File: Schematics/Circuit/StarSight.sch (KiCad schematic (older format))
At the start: 1 part

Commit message: Add last year code and schematic base
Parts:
- removed SH?: ARDUINO_MEGA, symbol ARDUINO_MEGA
- added P?: CONN_13X2, Pin_Headers:Pin_Header_Straight_2x13, symbol CONN_13X2
- added SH?: ARDUINO_MEGA, symbol ARDUINO_MEGA
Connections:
- net labels added: +3.3V, +5V, GND, GPIO0(SDA), GPIO1(SCL), GPIO10(MOSI), GPIO11(SCLK), GPIO17, GPIO18, GPIO21, GPIO22, GPIO23, GPIO24, GPIO25, GPIO4, GPIO7(CE1), GPIO8(CE0), GPIO9(MISO), RXD, TXD
- wire segments 0 -> 23
- no-connect marks 0 -> 6
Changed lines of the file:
@@
 LIBS:shield_arduino
 LIBS:StarSight-cache
+LIBS:raspberrypi-gpio-cache
 EELAYER 27 0
 EELAYER END
@@
 Sheet 1 1
 Title ""
-Date "14 dec 2017"
+Date "17 dec 2017"
 Rev ""
 Comp ""
@@
 $Comp
 L ARDUINO_MEGA SH?
-U 1 1 5A3242BC
-P 3200 4000
-F 0 "SH?" H 3200 4525 60  0000 C CNN
-F 1 "ARDUINO_MEGA" H 3200 4725 60  0000 C CNN
-F 2 "" H 2250 4300 60  0000 C CNN
-F 3 "" H 2250 4300 60  0000 C CNN
-	1    3200 4000
+U 1 1 5A367445
+P 8450 3450
+F 0 "SH?" H 8450 3975 60  0000 C CNN
+F 1 "ARDUINO_MEGA" H 8450 4175 60  0000 C CNN
+F 2 "" H 7500 3750 60  0000 C CNN
+F 3 "" H 7500 3750 60  0000 C CNN
+	1    8450 3450
 	1    0    0    -1
 $EndComp
+$Comp
+L CONN_13X2 P?
+U 1 1 5A367446
+P 2400 1800
+F 0 "P?" H 2400 2500 60  0000 C CNN
+F 1 "CONN_13X2" V 2400 1800 50  0000 C CNN
+F 2 "Pin_Headers:Pin_Header_Straight_2x13" H 2400 1100 30  0000 C CNN
+F 3 "" H 2400 1800 60  0001 C CNN
+	1    2400 1800
+	1    0    0    -1
+$EndComp
+$Comp
+L +3.3V #PWR?
+U 1 1 5A367447
+P 1900 1050
+F 0 "#PWR?" H 1900 900 50  0001 C CNN
+F 1 "+3.3V" H 1900 1190 50  0000 C CNN
+F 2 "" H 1900 1050 50  0000 C CNN
+F 3 "" H 1900 1050 50  0000 C CNN
+	1    1900 1050
+	1    0    0    -1
+$EndComp
+Wire Wire Line
+	1900 1050 1900 1200
+Wire Wire Line
+	1900 1200 2000 1200
+$Comp
+L +5V #PWR?
+U 1 1 5A367448
+P 2900 1050
+F 0 "#PWR?" H 2900 900 50  0001 C CNN
+F 1 "+5V" H 2900 1190 50  0000 C CNN
+F 2 "" H 2900 1050 50  0000 C CNN
+F 3 "" H 2900 1050 50  0000 C CNN
+	1    2900 1050
+	1    0    0    -1
+$EndComp
+Wire Wire Line
+	2900 1050 2900 1200
+Wire Wire Line
+	2900 1200 2800 1200
+NoConn ~ 2800 1300
+Wire Wire Line
+	2000 1300 1250 1300
+Wire Wire Line
+	2000 1400 1250 1400
+Text Label 1250 1300 0    60   ~ 0
+GPIO0(SDA)
+Text Label 1250 1400 0    60   ~ 0
+GPIO1(SCL)
+Wire Wire Line
+	2000 1500 1250 1500
+Text Label 1250 1500 0    60   ~ 0
+GPIO4
+NoConn ~ 2000 1600
+Wire Wire Line
+	2000 1700 1250 1700
+Wire Wire Line
+	2000 1800 1250 1800
+Wire Wire Line
+	2000 1900 1250 1900
+Text Label 1250 1700 0    60   ~ 0
+GPIO17
+Text Label 1250 1800 0    60   ~ 0
+GPIO21
+Text Label 1250 1900 0    60   ~ 0
+GPIO22
+NoConn ~ 2000 2000
+Wire Wire Line
+	2000 2100 1250 2100
+Wire Wire Line
+	2000 2200 1250 2200
+Wire Wire Line
+	2000 2300 1250 2300
+Text Label 1250 2100 0    60   ~ 0
+GPIO10(MOSI)
+Text Label 1250 2200 0    60   ~ 0
+GPIO9(MISO)
+Text Label 1250 2300 0    60   ~ 0
+GPIO11(SCLK)
+NoConn ~ 2000 2400
+$Comp
+L GND #PWR?
+U 1 1 5A367449
+P 2900 2500
+F 0 "#PWR?" H 2900 2250 50  0001 C CNN
+F 1 "GND" H 2900 2350 50  0000 C CNN
+F 2 "" H 2900 2500 50  0000 C CNN
+F 3 "" H 2900 2500 50  0000 C CNN
+	1    2900 2500
+	1    0    0    -1
+$EndComp
+Wire Wire Line
+	2900 2500 2900 1400
+Wire Wire Line
+	2900 1400 2800 1400
+Wire Wire Line
+	2800 1500 3500 1500
+Wire Wire Line
+	2800 1600 3500 1600
+Text Label 3500 1500 2    60   ~ 0
+TXD
+Text Label 3500 1600 2    60   ~ 0
+RXD
+Wire Wire Line
+	2800 1700 3500 1700
+Text Label 3500 1700 2    60   ~ 0
+GPIO18
+NoConn ~ 2800 1800
+Wire Wire Line
+	2800 1900 3500 1900
+Wire Wire Line
+	2800 2000 3500 2000
+Text Label 3500 1900 2    60   ~ 0
+GPIO23
+Text Label 3500 2000 2    60   ~ 0
+GPIO24
+NoConn ~ 2800 2100
+Wire Wire Line
+	2800 2200 3500 2200
+Text Label 3500 2200 2    60   ~ 0
+GPIO25
+Wire Wire Line
+	2800 2300 3500 2300
+Wire Wire Line
+	2800 2400 3500 2400
+Text Label 3500 2300 2    60   ~ 0
+GPIO8(CE0)
+Text Label 3500 2400 2    60   ~ 0
+GPIO7(CE1)
 $EndSCHEMATC

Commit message: Add the rest of the schematic
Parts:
- removed SH?: ARDUINO_MEGA, symbol ARDUINO_MEGA
- added C1, C2: 10 uF, ~, symbol C
- added C3: 100 nF, ~, symbol C
- added J1: Power, symbol Conn_01x02
- added J2: Line1, asd, symbol Conn_01x03
- added J3: Line2, asd, symbol Conn_01x03
- added J4: Line3, asd, symbol Conn_01x03
- added J5: Line4, asd, symbol Conn_01x03
- added J6: Line5, asd, symbol Conn_01x03
- added J? (x4): ultSound1, symbol Conn_01x04
- added J? (x5): IR1, asd, symbol Conn_01x03
- added SH?: ARDUINO_MEGA, symbol ARDUINO_MEGA
- added U?: LM1084IT-5.0/NOPB, TO-220, symbol LM1084IT-5.0/NOPB
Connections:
- net labels removed: +3.3V
- wire segments 23 -> 159
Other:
- moved on the sheet: P?

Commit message: Add pcb layout
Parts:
- removed J1: Power, symbol Conn_01x02
- removed SH?: ARDUINO_MEGA, symbol ARDUINO_MEGA
- added P2: Power, symbol CONN_2
- added SHIELD1: ARDUINO_MEGA_SHIELD, symbol ARDUINO_MEGA_SHIELD
- gave numbers to parts that had none: 11
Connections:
- wire segments 159 -> 165

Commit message: Add switched regulator and motors
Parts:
- removed U1: LM1084IT-5.0/NOPB, TO-220, symbol LM1084IT-5.0/NOPB
- added D1: 1n5824, symbol D_Schottky
- added D2, D3: D, Diodes_THT:D_DO-35_SOD27_P5.08mm_Vertical_KathodeUp, symbol D
- added IC1: LM2956-5V, symbol LM2956-5V
- added J16, J17: Conn_01x02, Pin_Headers:Pin_Header_Straight_1x02_Pitch2.54mm, symbol Conn_01x02
- added K1, K2: M1BS5V2-05T, Relays_THT:Relay_DPDT_Finder_40.52, symbol RSM822
- added L1: 33 uH, symbol L
- added Q1, Q2: Q_NMOS_GDS, Pin_Headers:Pin_Header_Straight_1x03_Pitch2.54mm, symbol Q_NMOS_GDS
- added R1, R2: 10k, Resistors_THT:R_Axial_DIN0207_L6.3mm_D2.5mm_P10.16mm_Horizontal, symbol R
- C1, C2, C3: symbol C -> C-RESCUE-StarSight
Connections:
- net GND: now also D1.2 (A), IC1.3 (GND), IC1.5 (ON/OFF), K1.11, K1.A1, K2.11, K2.A1, R1.1, R2.1
- net at C2.2, C3.2, P1.2 (P2): now also IC1.4 (FEEDBACK), L1.2
- net at SHIELD1.10: now also Q2.1 (G), R2.2
- net at SHIELD1.11: now also K2.A2
- net at SHIELD1.12: now also Q1.1 (G), R1.2
- net at SHIELD1.13: now also K1.A2
- net +12V: now reaches C1.2, P2.2 (PM), SHIELD1.V_IN
- net +12V: now also IC1.1 (VIN), Q1.3 (S), Q2.3 (S)
- new net: D1.1 (K), IC1.2 (OUT), L1.1
- new net: D2.2 (A), Q2.2 (D)
- new net: D2.1 (K), K2.21
- new net: J16.1 (Pin_1), K2.12, K2.24
- new net: J16.2 (Pin_2), K2.14, K2.22
- new net: J17.1 (Pin_1), K1.12, K1.24
- new net: J17.2 (Pin_2), K1.14, K1.22
- new net: D3.1 (K), K1.21
- new net: D3.2 (A), Q1.2 (D)
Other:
- moved on the sheet: C2, C3

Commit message: Fix footprint missing
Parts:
- D1: footprint (none) -> Diodes_THT:D_DO-201_P15.24mm_Horizontal
- IC1: footprint (none) -> Pin_Headers:Pin_Header_Straight_1x05_Pitch2.54mm
- L1: footprint (none) -> Diodes_THT:D_5W_P5.08mm_Vertical_KathodeUp
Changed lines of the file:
@@
 F 0 "IC1" H 2950 4050 60  0000 C CNN
 F 1 "LM2956-5V" H 3350 4050 60  0000 C CNN
-F 2 "" H 2950 4050 60  0001 C CNN
+F 2 "Pin_Headers:Pin_Header_Straight_1x05_Pitch2.54mm" H 2950 4050 60  0001 C CNN
 F 3 "" H 2950 4050 60  0001 C CNN
 	1    3250 3800
@@
 F 0 "L1" V 3100 4500 50  0000 C CNN
 F 1 "33 uH" V 3225 4500 50  0000 C CNN
-F 2 "" H 3150 4500 50  0001 C CNN
+F 2 "Diodes_THT:D_5W_P5.08mm_Vertical_KathodeUp" H 3150 4500 50  0001 C CNN
 F 3 "" H 3150 4500 50  0001 C CNN
 	1    3150 4500
@@
 F 0 "D1" H 2950 4450 50  0000 C CNN
 F 1 "1n5824" H 2950 4250 50  0000 C CNN
-F 2 "" H 2950 4350 50  0001 C CNN
+F 2 "Diodes_THT:D_DO-201_P15.24mm_Horizontal" H 2950 4350 50  0001 C CNN
 F 3 "" H 2950 4350 50  0001 C CNN
 	1    2950 4350

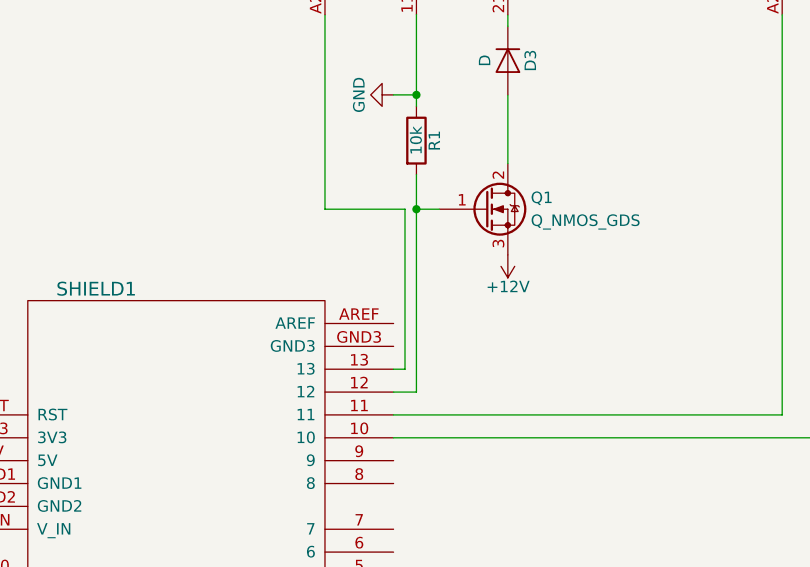
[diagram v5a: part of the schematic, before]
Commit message: Fix pcb power suply and motors
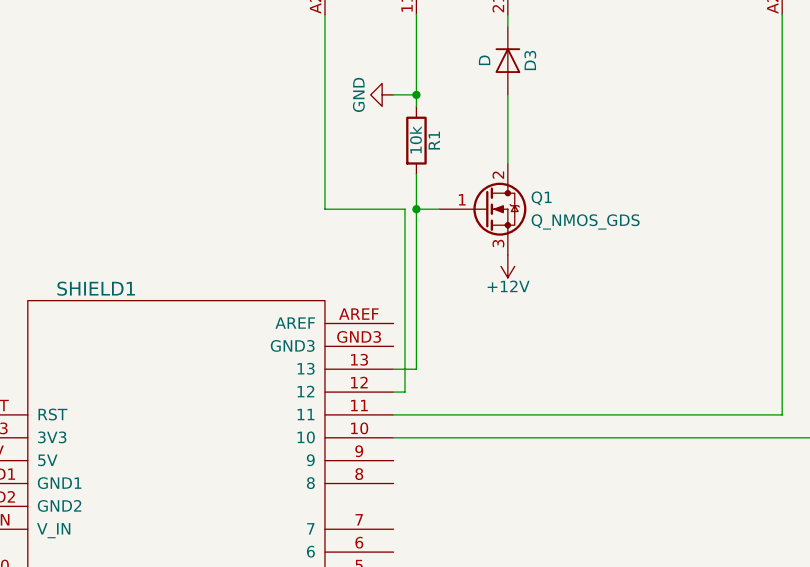
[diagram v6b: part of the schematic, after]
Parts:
- K1: footprint Relays_THT:Relay_DPDT_Finder_40.52 -> Relays_THT:Relay_DPDT_Omron_G5V-2
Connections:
- net at Q1.1 (G), R1.2: now also SHIELD1.13; no longer SHIELD1.12
- net at K1.A2: now also SHIELD1.12; no longer SHIELD1.13
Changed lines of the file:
@@
 F 0 "K1" H 10400 2100 50  0000 L CNN
 F 1 "M1BS5V2-05T" H 10400 2000 50  0000 L CNN
-F 2 "Relays_THT:Relay_DPDT_Finder_40.52" H 11100 1920 50  0001 C CNN
+F 2 "Relays_THT:Relay_DPDT_Omron_G5V-2" H 11100 1920 50  0001 C CNN
 F 3 "" H 9550 1950 50  0001 C CNN
 	1    9550 1950
@@
 $EndComp
 Wire Wire Line
-	9650 3900 9750 3900
-Wire Wire Line
-	9750 3900 9750 2950
-Wire Wire Line
 	9750 3100 9850 3100
 Connection ~ 9750 3100
@@
 	9350 1400 9350 1650
 Wire Wire Line
-	9650 3800 9700 3800
-Wire Wire Line
-	9700 3800 9700 3100
+	9650 3800 9750 3800
 Wire Wire Line
 	9700 3100 9350 3100
 Wire Wire Line
 	9350 3100 9350 2250
+Wire Wire Line
+	9750 3800 9750 2950
+Wire Wire Line
+	9650 3900 9700 3900
+Wire Wire Line
+	9700 3900 9700 3100
 $EndSCHEMATC

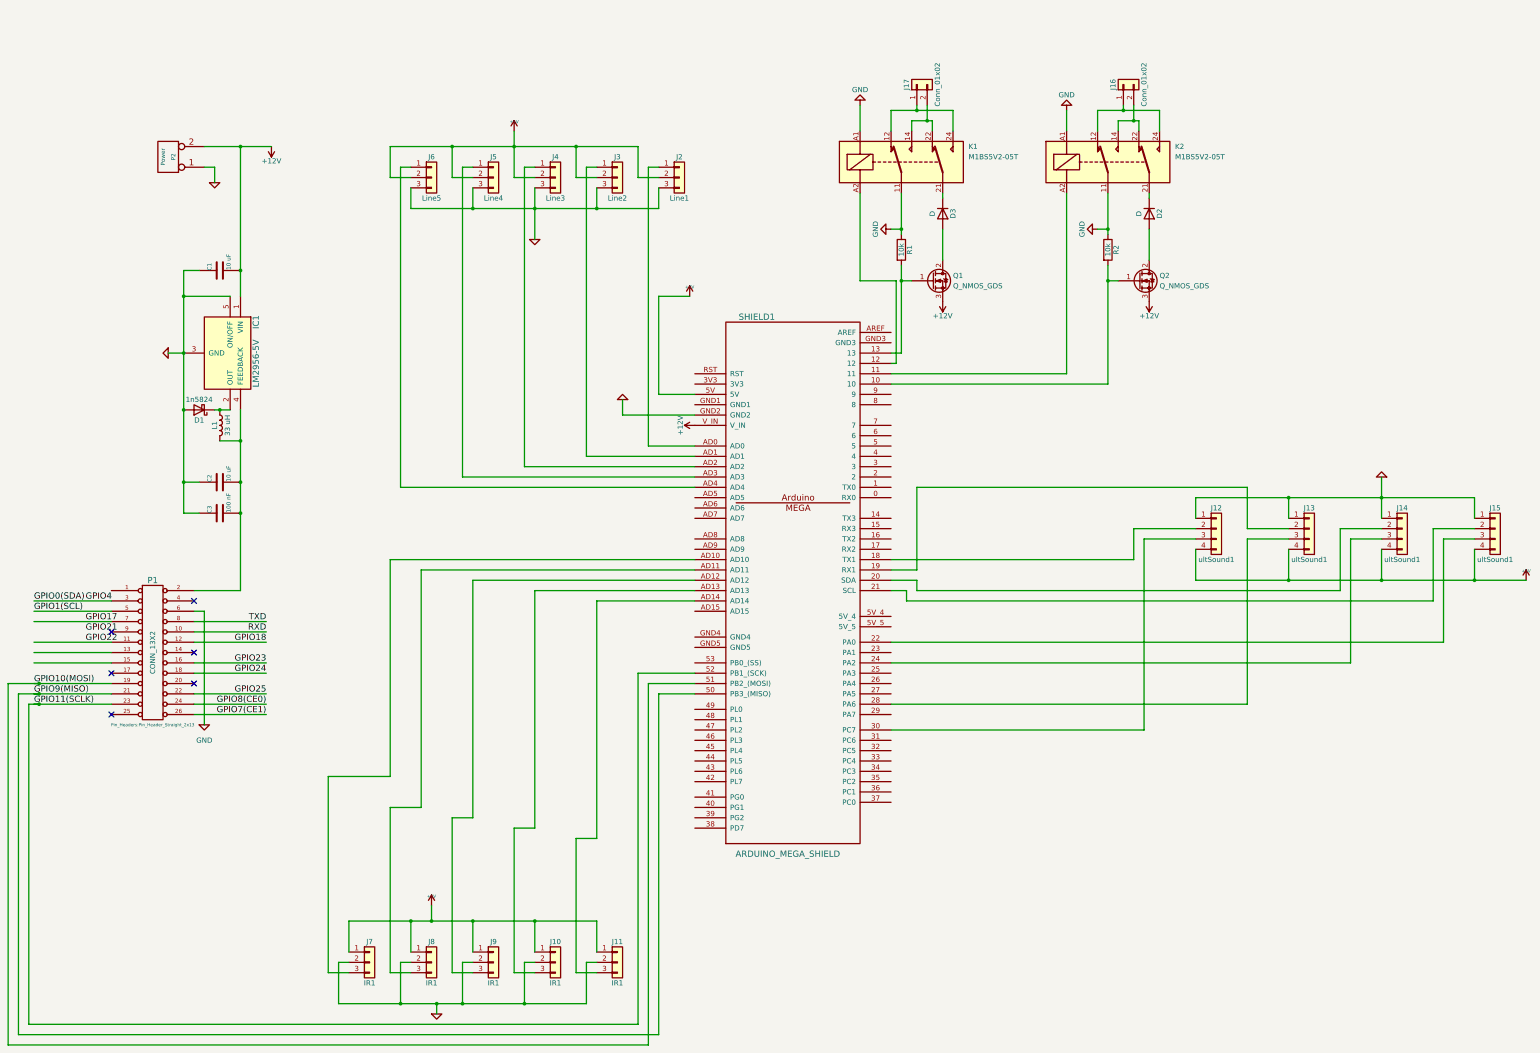
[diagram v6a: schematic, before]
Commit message: Fix relays and board size
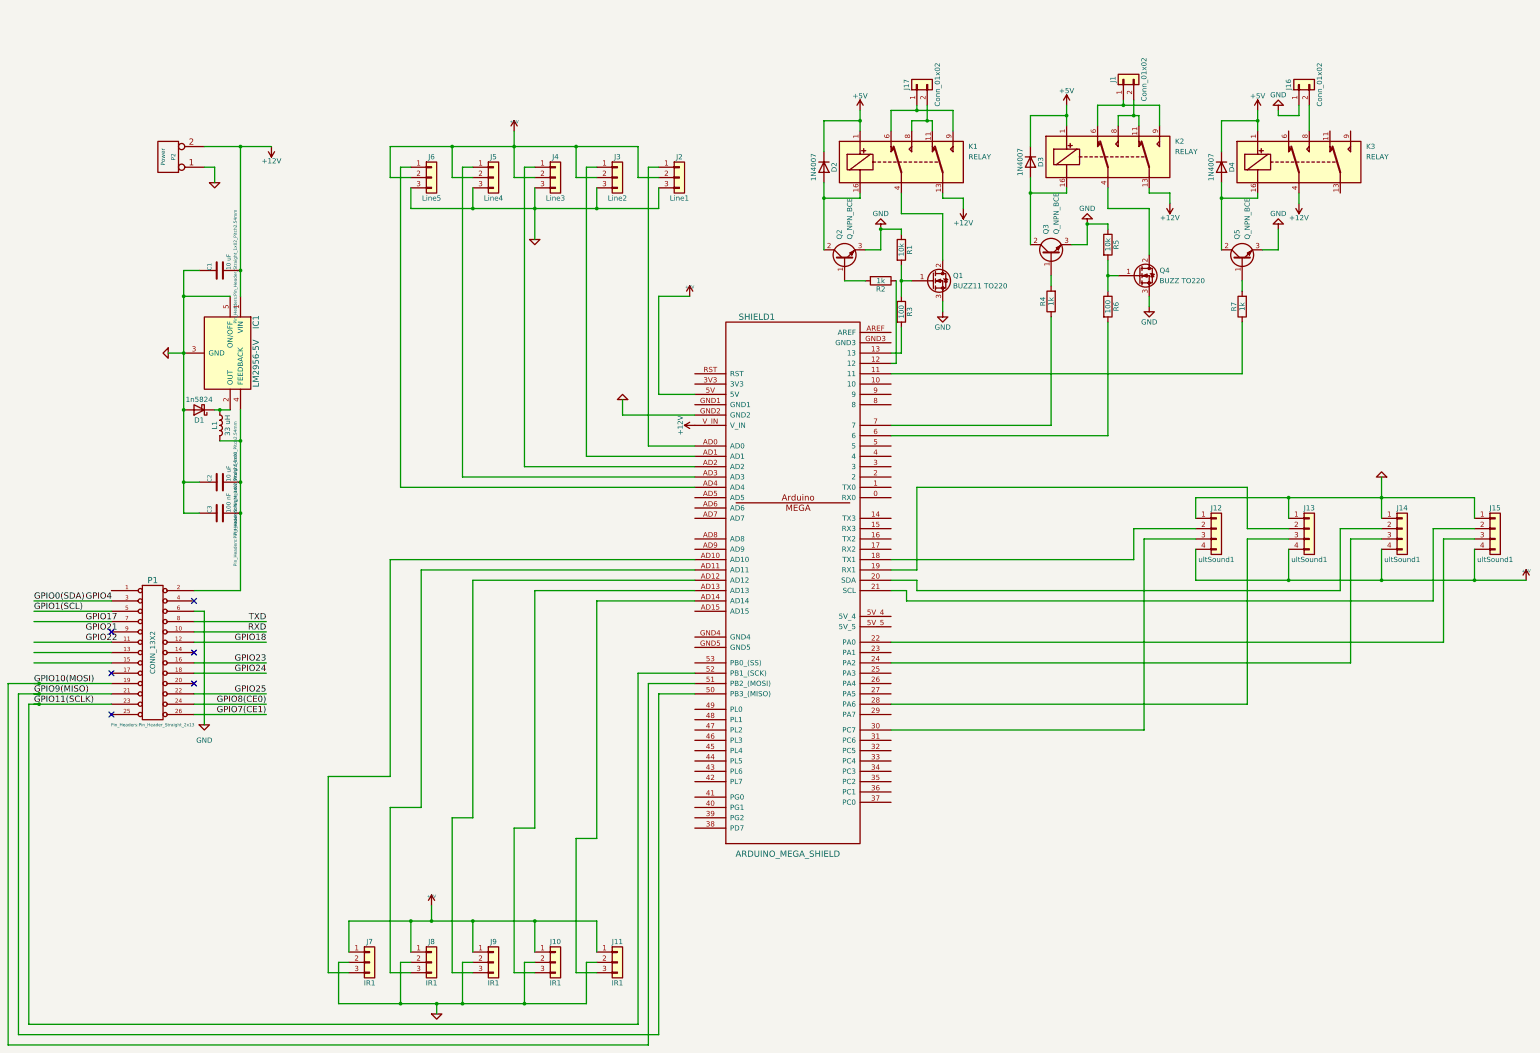
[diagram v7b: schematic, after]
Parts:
- removed K1: M1BS5V2-05T, Relays_THT:Relay_DPDT_Omron_G5V-2, symbol RSM822
- removed K2: M1BS5V2-05T, Relays_THT:Relay_DPDT_Finder_40.52, symbol RSM822
- removed Q2: Q_NMOS_GDS, Pin_Headers:Pin_Header_Straight_1x03_Pitch2.54mm, symbol Q_NMOS_GDS
- added D4: 1N4007, Diodes_THT:D_T-1_P10.16mm_Horizontal, symbol D
- added J1: Conn_01x02, Pin_Headers:Pin_Header_Straight_1x02_Pitch2.54mm, symbol Conn_01x02
- added K1, K2, K3: RELAY, Relays_THT:Relay_DPDT_Omron_G5V-2, symbol RELAY
- added Q2, Q3, Q5: Q_NPN_BCE, Pin_Headers:Pin_Header_Straight_1x03_Pitch1.27mm, symbol Q_NPN_BCE
- added Q4: BUZZ TO220, Pin_Headers:Pin_Header_Straight_1x03_Pitch2.54mm, symbol Q_NMOS_GDS
- added R3, R6: 100, Resistors_THT:R_Axial_DIN0414_L11.9mm_D4.5mm_P20.32mm_Horizontal, symbol R
- added R4, R7: 1k, Resistors_THT:R_Axial_DIN0414_L11.9mm_D4.5mm_P20.32mm_Horizontal, symbol R
- added R5: 10k, Resistors_THT:R_Axial_DIN0414_L11.9mm_D4.5mm_P20.32mm_Horizontal, symbol R
- C1, C2, C3: footprint ~ -> Pin_Headers:Pin_Header_Straight_1x02_Pitch2.54mm
- D2, D3: value D -> 1N4007; footprint Diodes_THT:D_DO-35_SOD27_P5.08mm_Vertical_KathodeUp -> Diodes_THT:D_T-1_P10.16mm_Horizontal
- IC1: footprint Pin_Headers:Pin_Header_Straight_1x05_Pitch2.54mm -> reg:TO170P470X1016X2092-5P
- J10, J11, J2, J3, J4, J5, J6, J7, J8, J9: footprint asd -> Pin_Headers:Pin_Header_Straight_1x03_Pitch2.54mm
- J12, J13, J14, J15: footprint (none) -> Pin_Headers:Pin_Header_Straight_1x04_Pitch2.54mm
- L1: footprint Diodes_THT:D_5W_P5.08mm_Vertical_KathodeUp -> Inductors_THT:L_Toroid_Vertical_L16.0mm_W8.0mm_P7.62mm
- P2: footprint (none) -> Pin_Headers:Pin_Header_Straight_1x02_Pitch2.54mm
- Q1: value Q_NMOS_GDS -> BUZZ11 TO220
- R1: footprint Resistors_THT:R_Axial_DIN0207_L6.3mm_D2.5mm_P10.16mm_Horizontal -> Resistors_THT:R_Axial_DIN0414_L11.9mm_D4.5mm_P20.32mm_Horizontal
- R2: value 10k -> 1k; footprint Resistors_THT:R_Axial_DIN0207_L6.3mm_D2.5mm_P10.16mm_Horizontal -> Resistors_THT:R_Axial_DIN0414_L11.9mm_D4.5mm_P20.32mm_Horizontal
- SHIELD1: footprint (none) -> arduino_shields:ARDUINO_MEGA_SHIELD
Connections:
- net +12V: now also K1.13, K2.13, K3.4; no longer Q1.3 (S)
- net +5V: now also D2.1 (K), D3.1 (K), D4.1 (K), K1.1, K2.1, K3.1
- net GND: now also J16.1 (Pin_1), Q1.3 (S), Q2.3 (E), Q3.3 (E), Q4.3 (S), Q5.3 (E), R5.1; no longer R2.1
- net at SHIELD1.10: no longer R2.2
- net at SHIELD1.11: now also R7.1
- net at SHIELD1.12: now also R2.1
- net at Q1.1 (G), R1.2: now also R3.1; no longer SHIELD1.13
- net at SHIELD1.6: now also R6.2
- net at SHIELD1.7: now also R4.1
- net at D2.2 (A): now also K1.16, Q2.2 (C)
- net at J16.2 (Pin_2): now also K3.8
- net at J17.1 (Pin_1): now also K1.6, K1.9
- net at J17.2 (Pin_2): now also K1.11, K1.8
- net at Q1.2 (D): now also K1.4; no longer D3.2 (A)
- new net: R3.2, SHIELD1.13
- new net: Q2.1 (B), R2.2
- new net: J1.1 (Pin_1), K2.6, K2.9
- new net: J1.2 (Pin_2), K2.11, K2.8
- new net: Q4.1 (G), R5.2, R6.1
- new net: K2.4, Q4.2 (D)
- new net: Q3.1 (B), R4.2
- new net: D3.2 (A), K2.16, Q3.2 (C)
- new net: Q5.1 (B), R7.2
- new net: D4.2 (A), K3.16, Q5.2 (C)
